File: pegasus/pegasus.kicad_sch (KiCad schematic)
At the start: 14 parts, among them IC2 Adafruit_MPL3115A2, IC3 Adafruit-BNO055-PCB, IC4 L70B-M39, IC5 L7805ACV, J1 Conn_01x02_Female, J2 Conn_01x02_Female, U1 Teensy4.1, U2 CON-SMA-EDGE-S, U3 CON-SMA-EDGE-S

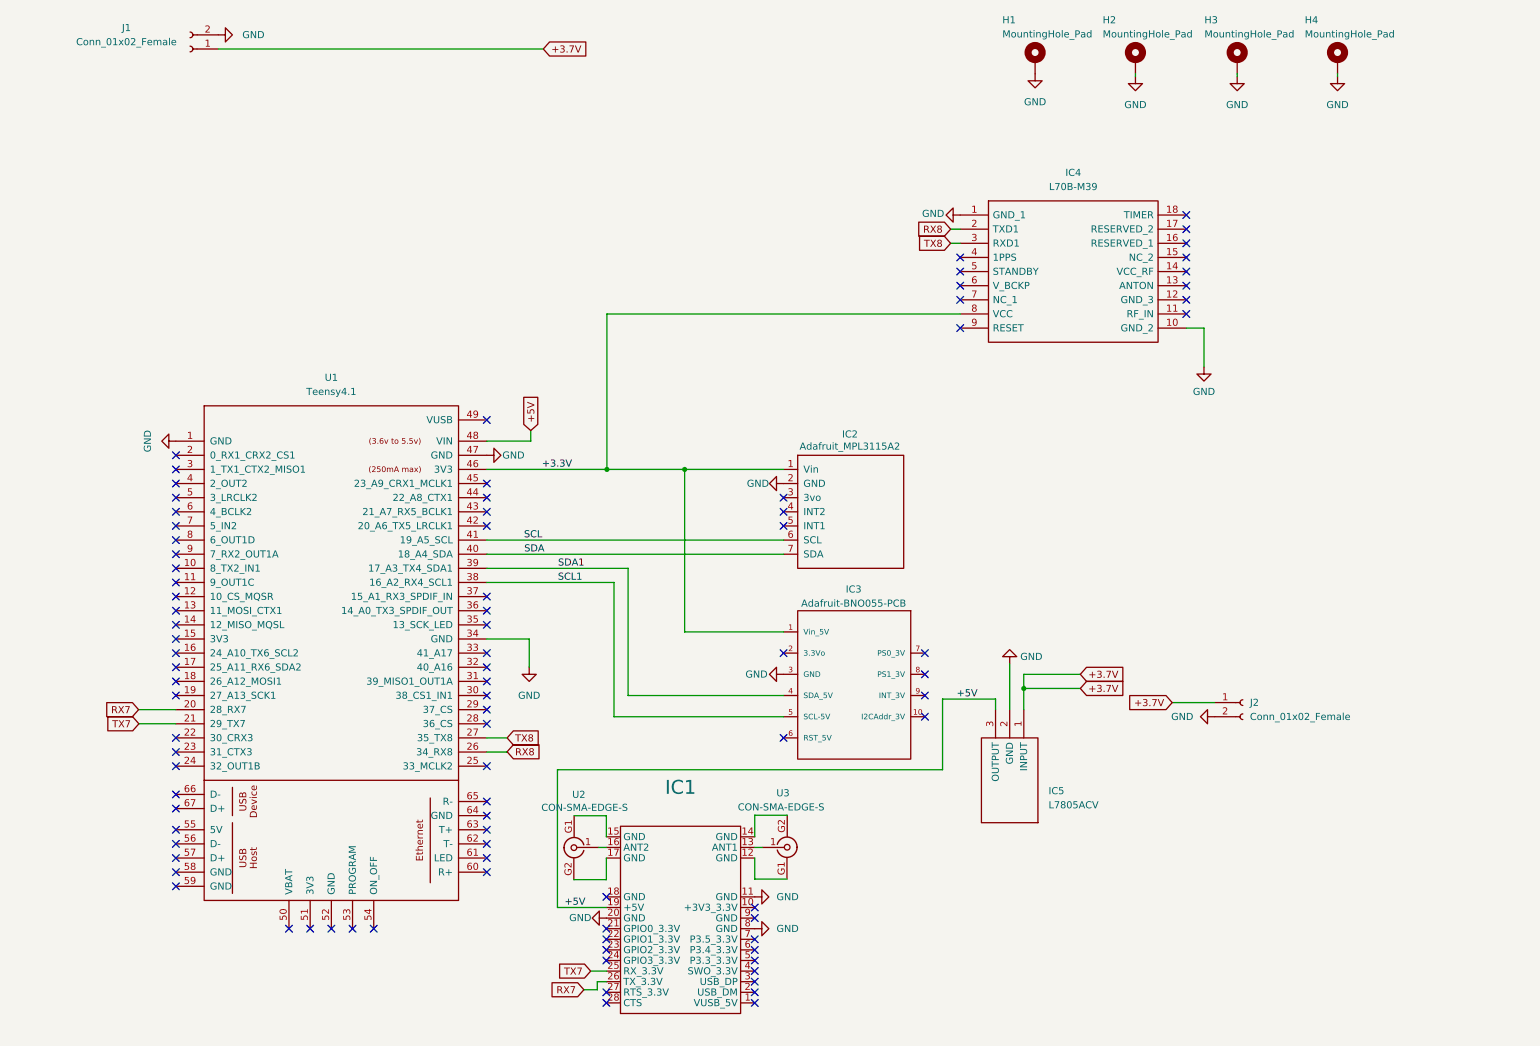
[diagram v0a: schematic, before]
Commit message: replace teensy 4.1 wih teensy 4, remove barometer and IMU
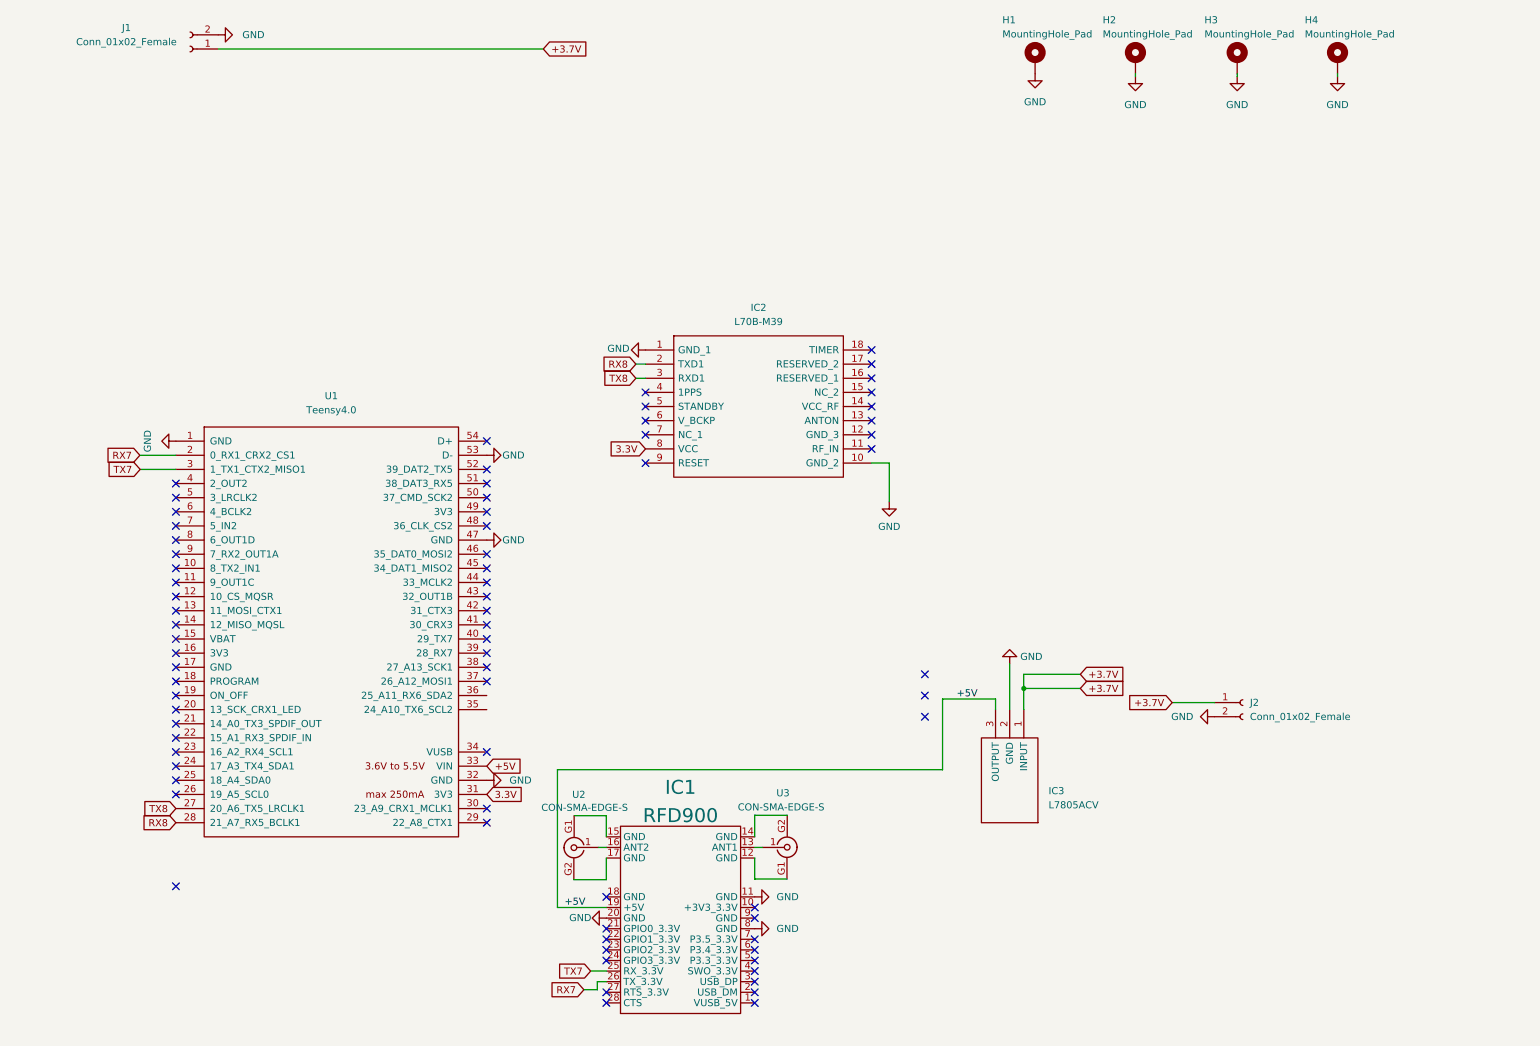
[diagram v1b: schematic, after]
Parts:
- removed IC2: Adafruit_MPL3115A2, Adafruit_MPL3115A2:1x07, symbol Adafruit_MPL3115A2:Adafruit_MPL3115A2
- removed IC3: Adafruit-BNO055-PCB, Adafruit_BNO055:adafruit_, symbol Adafruit_BNO055:Adafruit-BNO055-PCB
- removed U1: Teensy4.1, Teensy_4.1:Teensy_4.1, symbol teensy:Teensy4.1
- added U1: Teensy4.0, Teensy:Teensy40, symbol teensy:Teensy4.0
- IC1: value (none) -> RFD900
- renumbered IC4 to IC2, IC5 to IC3
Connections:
- net +5V: now also U1.33 (VIN)
- net GND: now also U1.1 (GND), U1.32 (GND), U1.47 (GND), U1.53 (D-)
- net RX7: now also U1.2 (0_RX1_CRX2_CS1)
- net RX8: now also U1.28 (21_A7_RX5_BCLK1)
- net TX7: now also U1.3 (1_TX1_CTX2_MISO1)
- net TX8: now also U1.27 (20_A6_TX5_LRCLK1)
- net +3.3V renamed 3.3V
- net 3.3V: now also U1.31 (3V3)
- no-connect marks 92 -> 75
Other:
- moved on the sheet: IC2

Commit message: replace sma-connectors with screw terminal with switch
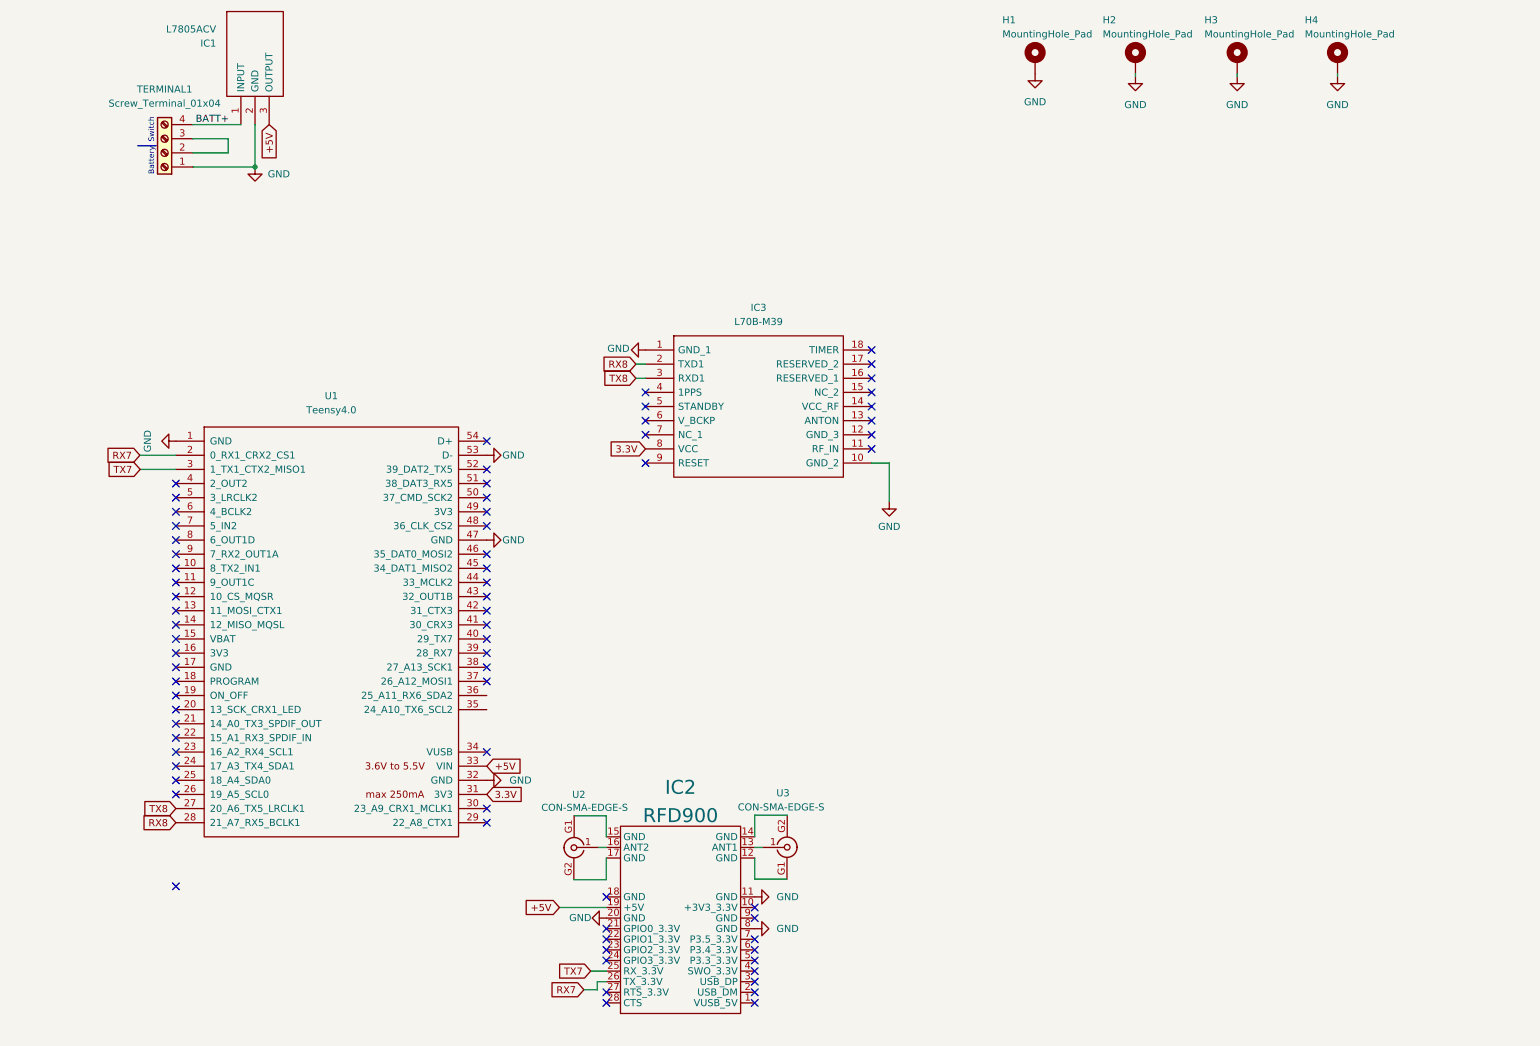
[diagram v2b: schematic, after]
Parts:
- removed J1, J2: Conn_01x02_Female, Connector_PinHeader_2.00mm:PinHeader_1x02_P2.00mm_Vertical, symbol Connector:Conn_01x02_Female
- added TERMINAL1: Screw_Terminal_01x04, RS-Components:SHDR4W100P0X500_1X4_2000X800X1000P, symbol Connector:Screw_Terminal_01x04
- renumbered IC3 to IC1, IC1 to IC2, IC2 to IC3
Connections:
- net GND: now also TERMINAL1.1 (Pin_1)
- net +3.7V renamed BATT+
- net BATT+: now also TERMINAL1.4 (Pin_4)
- new net: TERMINAL1.2 (Pin_2), TERMINAL1.3 (Pin_3)
- no-connect marks 75 -> 72
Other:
- note added: "Battery"
- note added: "Switch"
- moved on the sheet: IC1
